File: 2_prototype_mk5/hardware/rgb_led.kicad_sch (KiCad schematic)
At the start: 2 parts

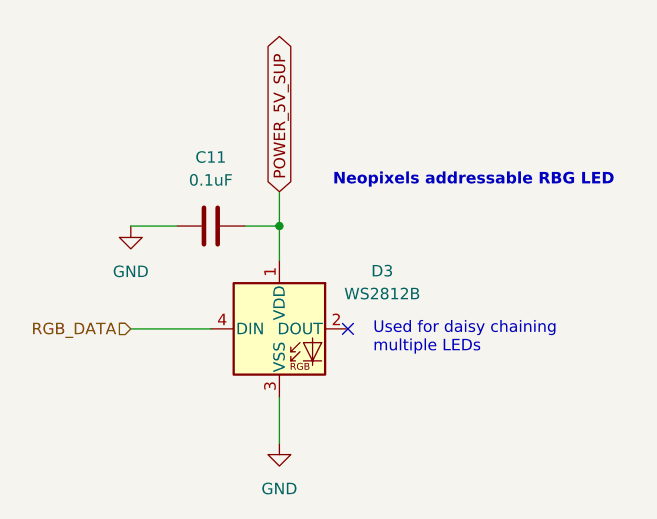
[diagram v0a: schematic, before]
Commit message: Major MKV redesign using embedded RP2350
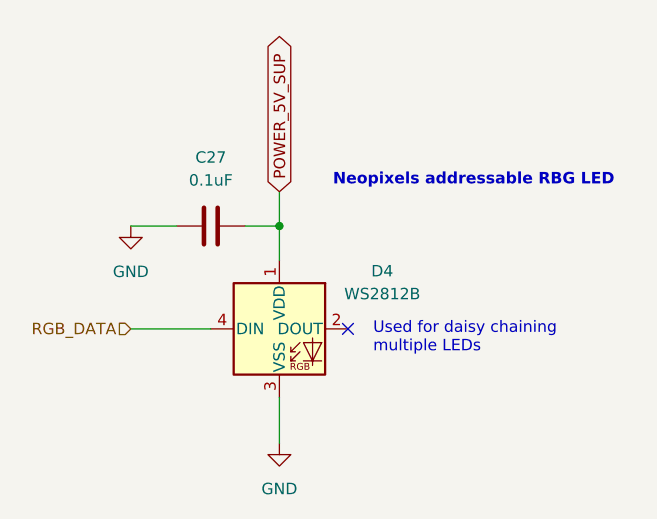
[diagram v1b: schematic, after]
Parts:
- renumbered C11 to C27, D3 to D4
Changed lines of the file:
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@@
 		(dnp no)
 		(fields_autoplaced yes)
-		(property "Reference" "#PWR041"
+		(property "Reference" "#PWR056"
 			(at 142.24 118.11 0)
 			(hide yes)
@@
 			(project "HDD Synth Prototype MK5"
 				(path "/1a22431a-ba36-40a0-9a7e-c2a82ec69c53/779dbbe7-9583-41dc-a633-b3a85967b109"
-					(reference "#PWR041")
+					(reference "#PWR056")
 					(unit 1)
 				)
@@
 		(dnp no)
 		(fields_autoplaced yes)
-		(property "Reference" "D3"
+		(property "Reference" "D4"
 			(at 153.67 92.6398 0)
 			(show_name no)
@@
 			(project "HDD Synth Prototype MK5"
 				(path "/1a22431a-ba36-40a0-9a7e-c2a82ec69c53/779dbbe7-9583-41dc-a633-b3a85967b109"
-					(reference "D3")
+					(reference "D4")
 					(unit 1)
 				)
@@
 		(dnp no)
 		(fields_autoplaced yes)
-		(property "Reference" "#PWR042"
+		(property "Reference" "#PWR055"
 			(at 125.73 93.98 0)
 			(hide yes)
@@
 			(project "HDD Synth Prototype MK5"
 				(path "/1a22431a-ba36-40a0-9a7e-c2a82ec69c53/779dbbe7-9583-41dc-a633-b3a85967b109"
-					(reference "#PWR042")
+					(reference "#PWR055")
 					(unit 1)
 				)
@@
 		(dnp no)
 		(fields_autoplaced yes)
-		(property "Reference" "C11"
+		(property "Reference" "C27"
 			(at 134.62 80.01 90)
 			(show_name no)
@@
 			(project "HDD Synth Prototype MK5"
 				(path "/1a22431a-ba36-40a0-9a7e-c2a82ec69c53/779dbbe7-9583-41dc-a633-b3a85967b109"
-					(reference "C11")
+					(reference "C27")
 					(unit 1)
 				)

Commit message: MKV: Add LCSC numbers and resolve DRC errors
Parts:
- C27: LCSC_Part_Number (none) -> C14663
- D4: LCSC_Part_Number (none) -> C2761795
